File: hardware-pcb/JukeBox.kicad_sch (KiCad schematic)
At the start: 80 parts, among them J1 USB4105-GF-A, Q1 Q_NPN_BEC, SW1 SW_SPST, SW10 SW_SPST, SW11 SW_SPST, SW12 SW_SPST, SW2 SW_SPST, SW3 SW_SPST, SW4 SW_SPST, SW5 SW_SPST, SW6 SW_SPST, SW7 SW_SPST, SW8 SW_SPST, SW9 SW_SPST, U1 NCP1117-3.3_SOT223, U2 W25Q16JVUXIQ TR, U3 RP2040, U4 st7789v, Y1 ECS-120-20-33-AEL-TR

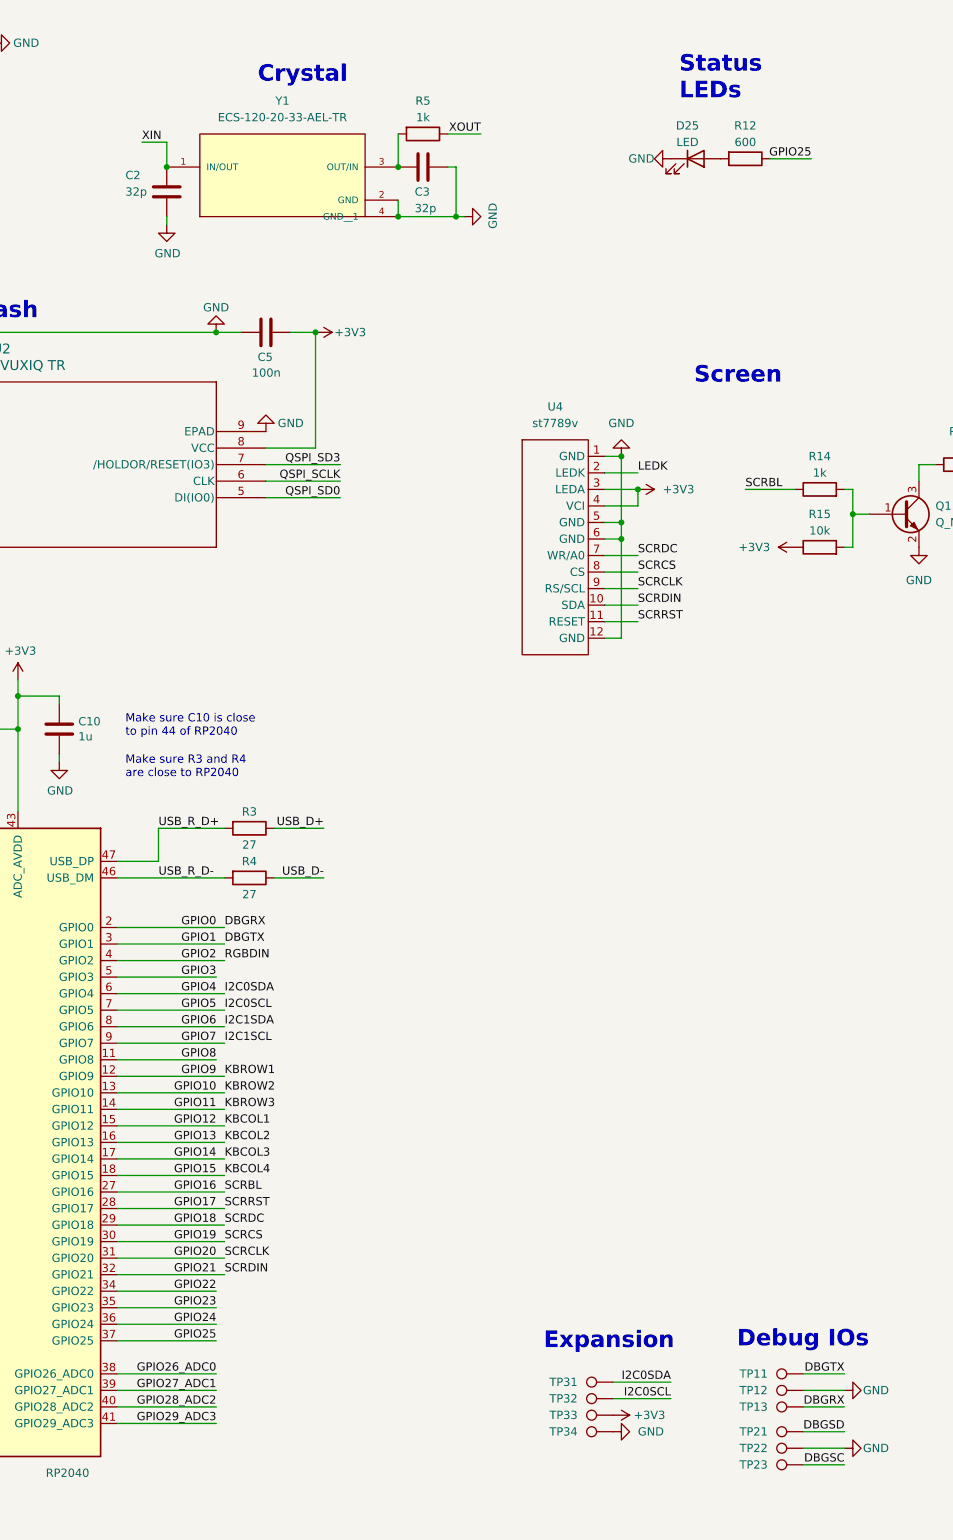
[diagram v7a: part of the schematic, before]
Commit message: switch to 2020 leds, switch to new key footprint, extend io connectors, update case geometry
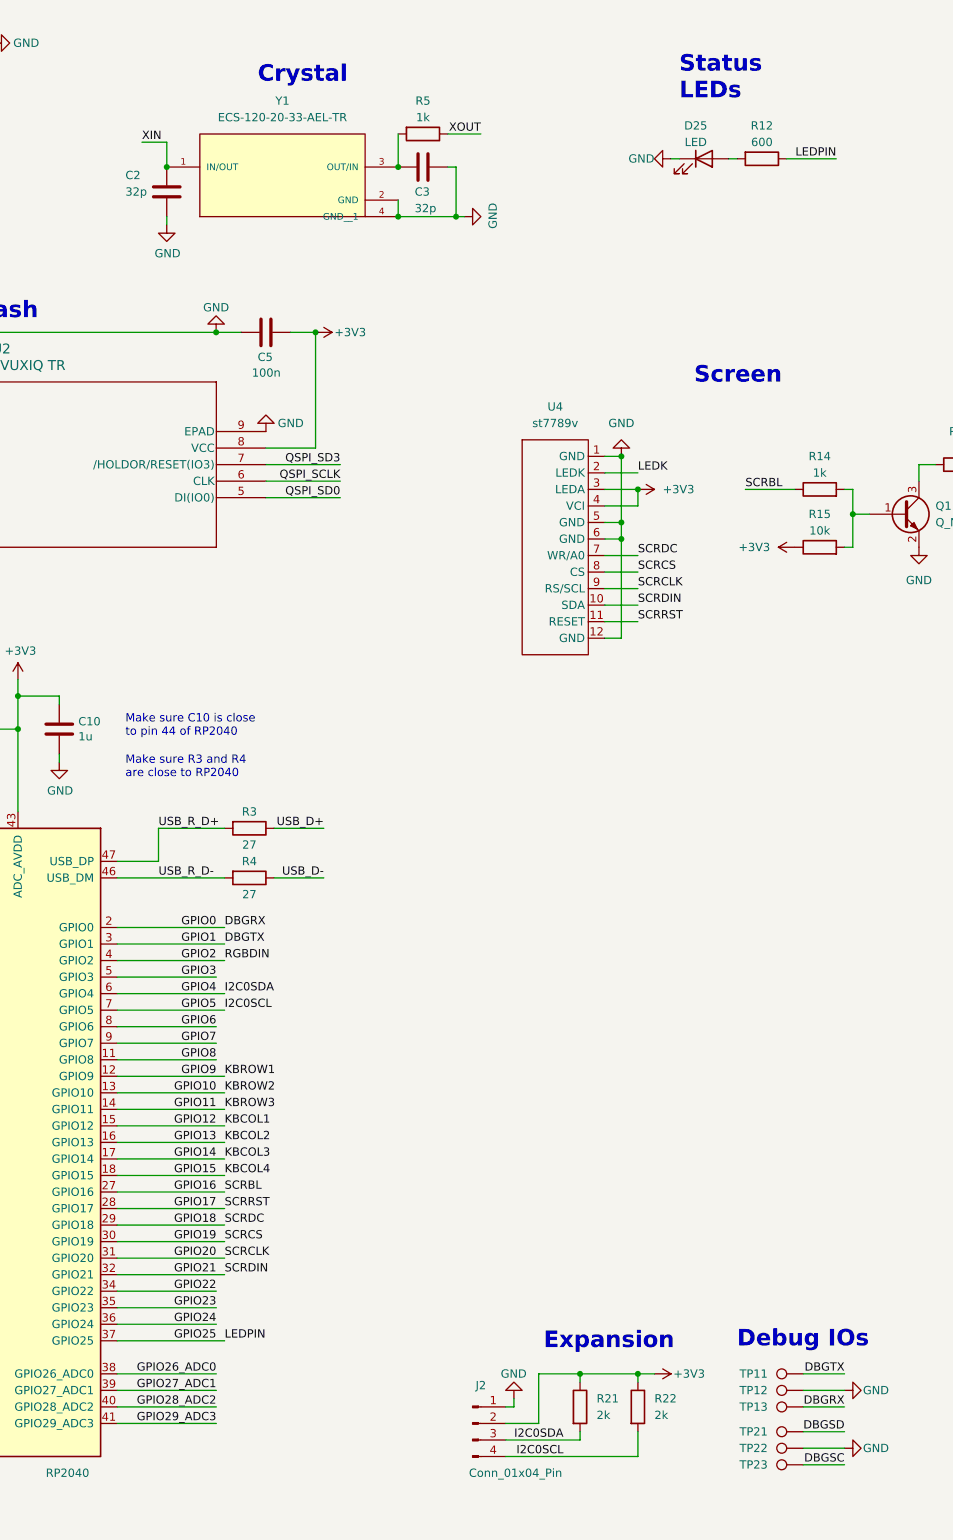
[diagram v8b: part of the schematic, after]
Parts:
- removed TP31, TP32, TP33, TP34: TestPoint, TestPoint:TestPoint_Pad_D1.5mm, symbol Connector:TestPoint
- added J2: Conn_01x04_Pin, Connector_JST:JST_SH_SM04B-SRSS-TB_1x04-1MP_P1.00mm_Horizontal, symbol Connector:Conn_01x04_Pin
- added R21, R22: 2k, Resistor_SMD:R_0805_2012Metric_Pad1.20x1.40mm_HandSolder, symbol Device:R
- J1: footprint RP2040_minimal:GCT_USB4105-GF-A -> JukeBox:GCT_USB4105-GF-A
- SW1, SW10, SW11, SW12, SW2, SW3, SW4, SW5, SW6, SW7, SW8, SW9: footprint RP2040_minimal:Kailh_Choc_MX_Key -> JukeBox:ALLKEY
- U3: footprint RP2040_minimal:RP2040-QFN-56 -> JukeBox:RP2040-QFN-56
- U4: footprint RP2040_minimal:st7789v -> JukeBox:st7789v
- Y1: footprint RP2040_minimal:XTAL_ECS-120-20-33-AEL-TR -> JukeBox:XTAL_ECS-120-20-33-AEL-TR
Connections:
- net +3V3: now also J2.2 (Pin_2), R21.1, R22.1
- net GND: now also J2.1 (Pin_1)
- net GPIO4: now also J2.3 (Pin_3), R21.2
- net GPIO5: now also J2.4 (Pin_4), R22.2
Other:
- moved on the sheet: D25, R12
